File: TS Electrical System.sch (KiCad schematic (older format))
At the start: 29 parts

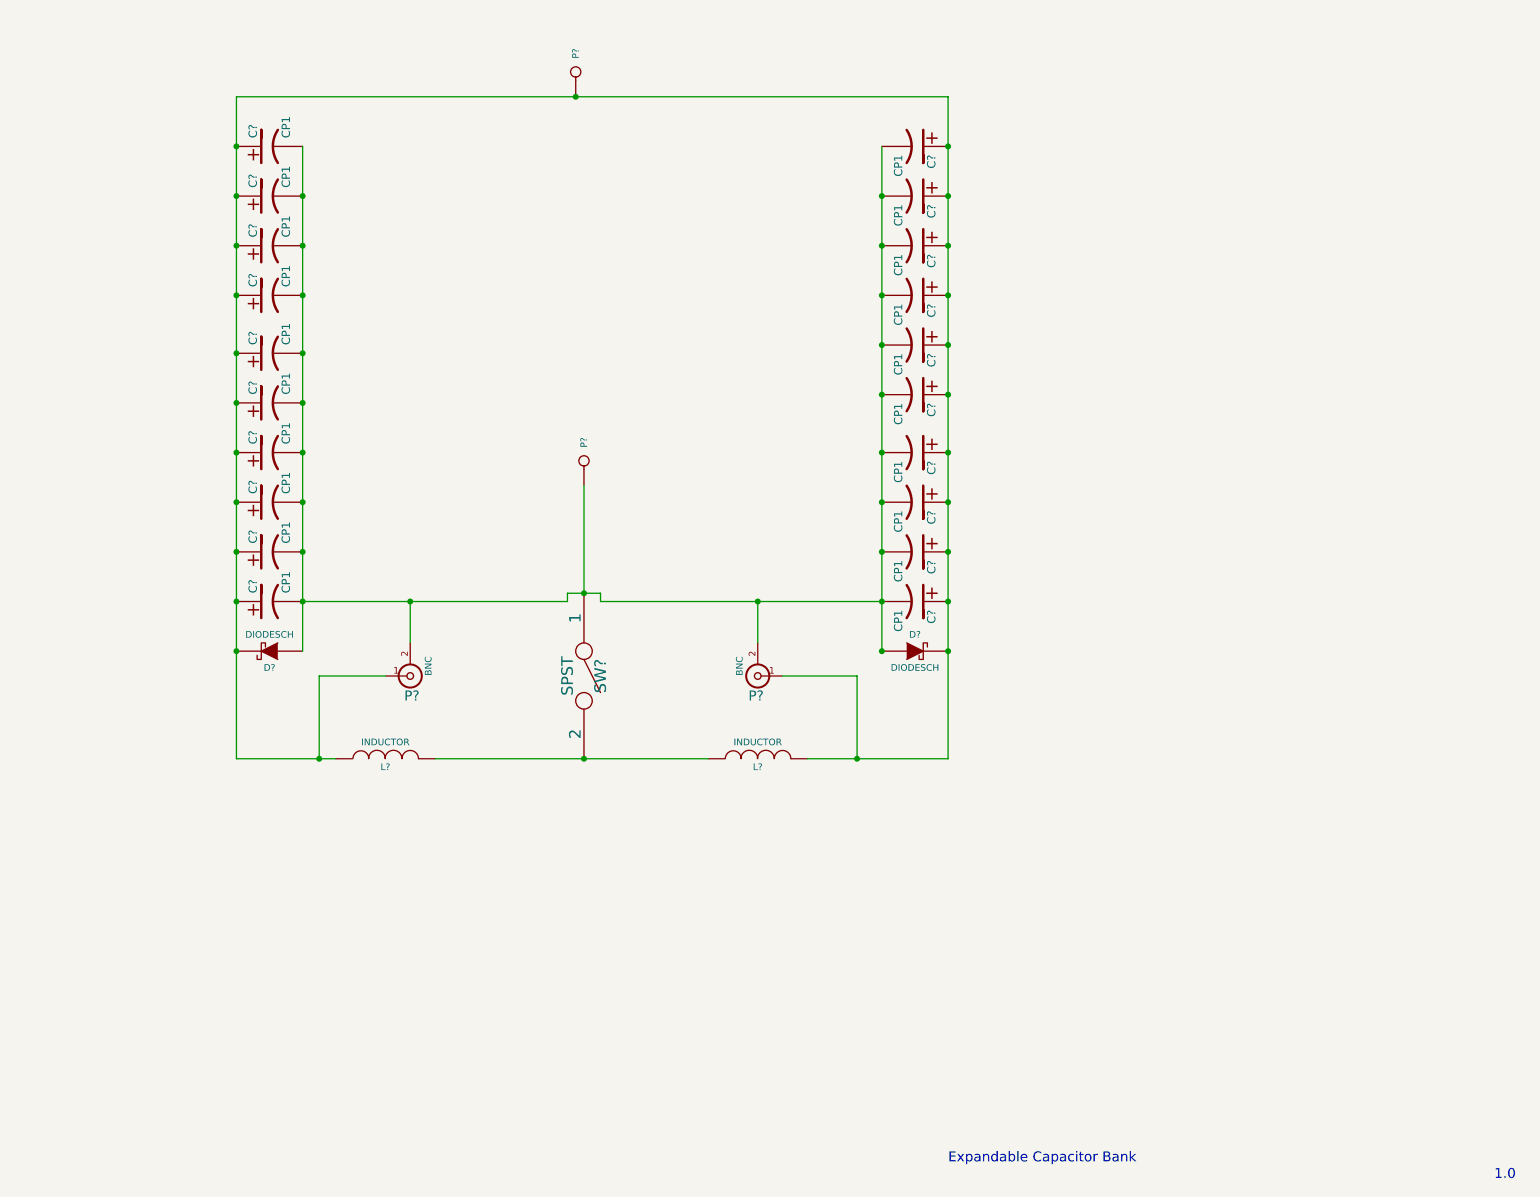
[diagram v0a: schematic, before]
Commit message: Associated Parts with Footprints, created footprints, and did part layout.
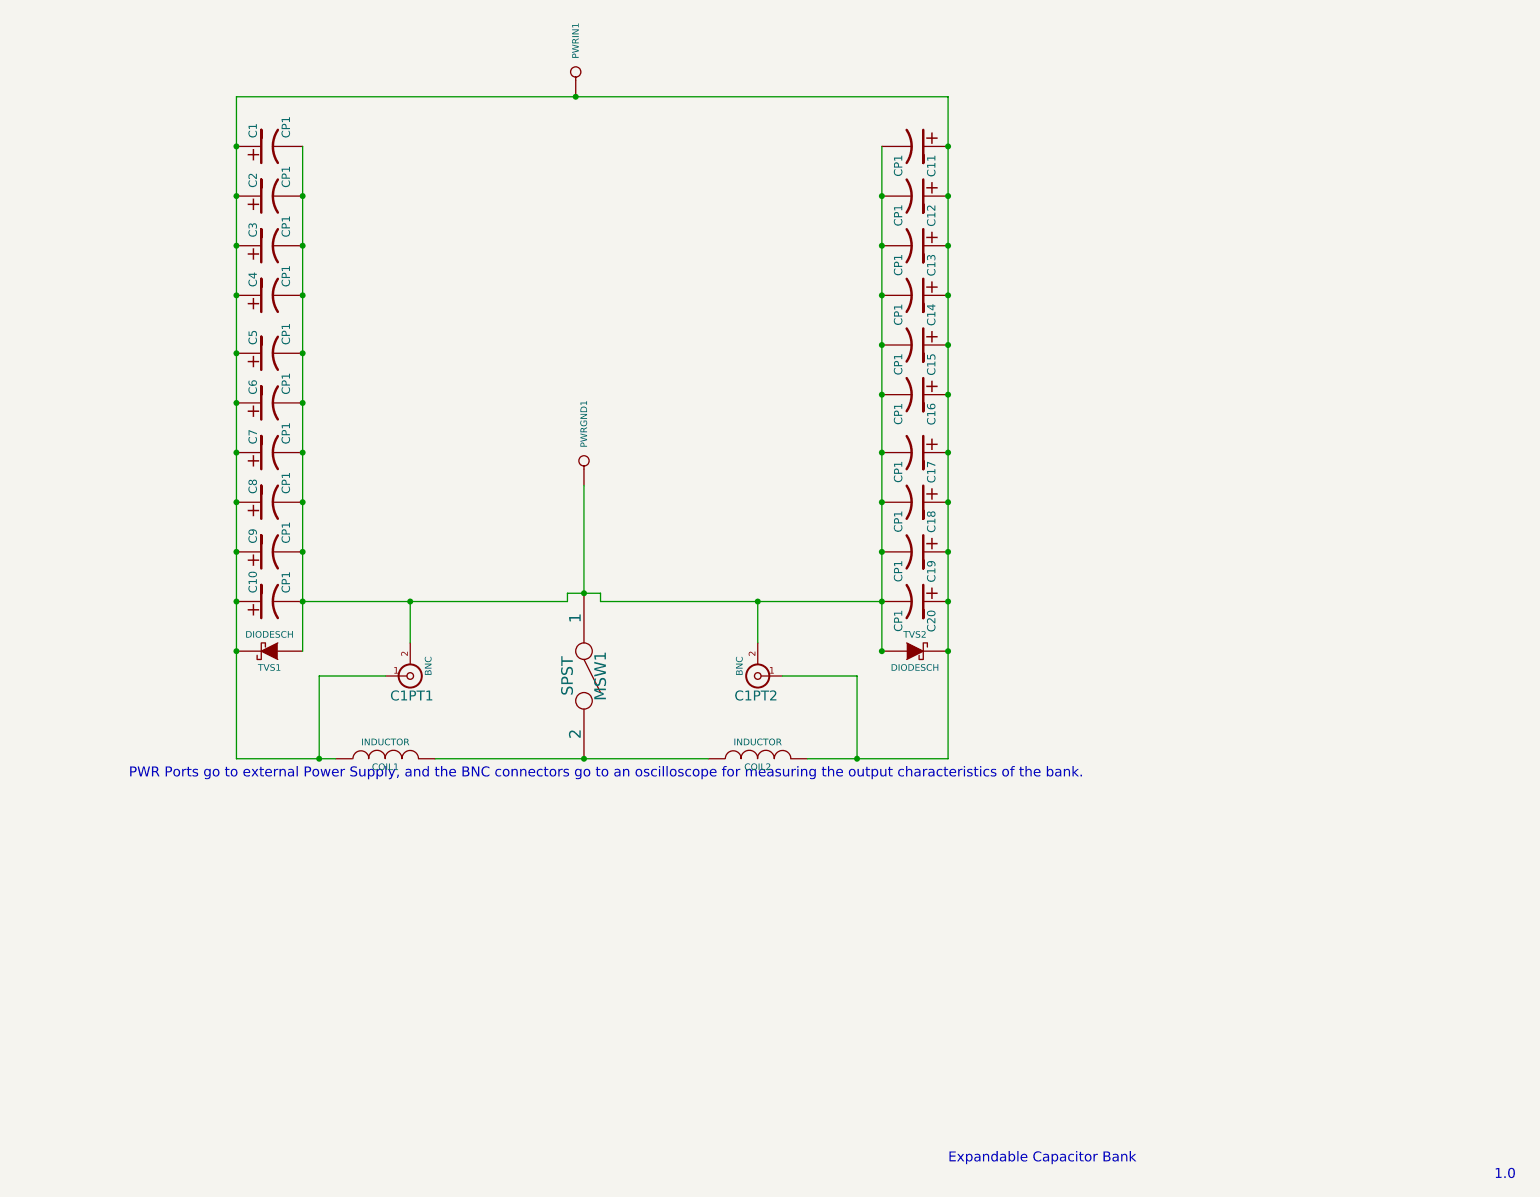
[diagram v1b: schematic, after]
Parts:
- gave numbers to parts that had none: 29
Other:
- note added: "PWR Ports go to external Power Supply, and the BNC connectors go to an oscilloscope for measuring the output characteristics of the bank.\n\n\n\n\n\n\n\n"
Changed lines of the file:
@@
-EESchema Schematic File Version 2  date Wed 30 Jul 2014 05:31:54 PM EDT
+EESchema Schematic File Version 2  date Wed 30 Jul 2014 05:36:56 PM EDT
 LIBS:power
 LIBS:device
@@
 Comment4 ""
 $EndDescr
+Text Notes 2400 5900 0    60   ~ 0
+PWR Ports go to external Power Supply, and the BNC connectors go to an oscilloscope for measuring the output characteristics of the bank.\n\n\n\n\n\n\n\n
 Connection ~ 5100 1100
 Connection ~ 3050 1400
@@
 	5150 3450 5150 4100
 $Comp
-L CONN_1 P?
+L CONN_1 PWRIN1
 U 1 1 53D96425
 P 5100 950
-F 0 "P?" H 5180 950 40  0000 L CNN
+F 0 "PWRIN1" H 5180 950 40  0000 L CNN
 F 1 "CONN_1" H 5100 1005 30  0001 C CNN
 	1    5100 950
@@
 $EndComp
 $Comp
-L CONN_1 P?
+L CONN_1 PWRGND1
 U 1 1 53D9641D
 P 5150 3300
-F 0 "P?" H 5230 3300 40  0000 L CNN
+F 0 "PWRGND1" H 5230 3300 40  0000 L CNN
 F 1 "CONN_1" H 5150 3355 30  0001 C CNN
 	1    5150 3300
@@
 1.0
 $Comp
-L BNC P?
+L BNC C1PT1
 U 1 1 53D9628A
 P 4100 4600
-F 0 "P?" H 4110 4720 60  0000 C CNN
+F 0 "C1PT1" H 4110 4720 60  0000 C CNN
 F 1 "BNC" V 4210 4540 40  0000 C CNN
 	1    4100 4600
@@
 $EndComp
 $Comp
-L BNC P?
+L BNC C1PT2
 U 1 1 53D9627A
 P 6200 4600
-F 0 "P?" H 6210 4720 60  0000 C CNN
+F 0 "C1PT2" H 6210 4720 60  0000 C CNN
 F 1 "BNC" V 6310 4540 40  0000 C CNN
 	1    6200 4600
@@
 $EndComp
 $Comp
-L SPST SW?
+L SPST MSW1
 U 1 1 53D96065
 P 5150 4600
-F 0 "SW?" H 5150 4700 70  0000 C CNN
+F 0 "MSW1" H 5150 4700 70  0000 C CNN
 F 1 "SPST" H 5150 4500 70  0000 C CNN
 	1    5150 4600
@@
 $EndComp
 $Comp
-L INDUCTOR L?
+L INDUCTOR COIL1
 U 1 1 53D961F9
 P 3950 5100
-F 0 "L?" V 3900 5100 40  0000 C CNN
+F 0 "COIL1" V 3900 5100 40  0000 C CNN
 F 1 "INDUCTOR" V 4050 5100 40  0000 C CNN
 	1    3950 5100
@@
 $EndComp
 $Comp
-L INDUCTOR L?
+L INDUCTOR COIL2
 U 1 1 53D961EB
 P 6200 5100
-F 0 "L?" V 6150 5100 40  0000 C CNN
+F 0 "COIL2" V 6150 5100 40  0000 C CNN
 F 1 "INDUCTOR" V 6300 5100 40  0000 C CNN
 	1    6200 5100
@@
 $EndComp
 $Comp
-L DIODESCH D?
+L DIODESCH TVS2
 U 1 1 53D96017
 P 7150 4450
-F 0 "D?" H 7150 4550 40  0000 C CNN
+F 0 "TVS2" H 7150 4550 40  0000 C CNN
 F 1 "DIODESCH" H 7150 4350 40  0000 C CNN
 	1    7150 4450
@@
 $EndComp
 $Comp
-L DIODESCH D?
+L DIODESCH TVS1
 U 1 1 53D9600F
 P 3250 4450
-F 0 "D?" H 3250 4550 40  0000 C CNN
+F 0 "TVS1" H 3250 4550 40  0000 C CNN
 F 1 "DIODESCH" H 3250 4350 40  0000 C CNN
 	1    3250 4450
@@
 $EndComp
 $Comp
-L CP1 C?
+L CP1 C20
 U 1 1 53D95FE6
 P 7150 4150
-F 0 "C?" H 7200 4250 50  0000 L CNN
+F 0 "C20" H 7200 4250 50  0000 L CNN
 F 1 "CP1" H 7200 4050 50  0000 L CNN
 	1    7150 4150
@@
 $EndComp
 $Comp
-L CP1 C?
+L CP1 C19
 U 1 1 53D95FE5
 P 7150 3850
-F 0 "C?" H 7200 3950 50  0000 L CNN
+F 0 "C19" H 7200 3950 50  0000 L CNN
 F 1 "CP1" H 7200 3750 50  0000 L CNN
 	1    7150 3850
@@
 $EndComp
 $Comp
-L CP1 C?
+L CP1 C17
 U 1 1 53D95FE4
 P 7150 3250
-F 0 "C?" H 7200 3350 50  0000 L CNN
+F 0 "C17" H 7200 3350 50  0000 L CNN
 F 1 "CP1" H 7200 3150 50  0000 L CNN
 	1    7150 3250
@@
 $EndComp
 $Comp
-L CP1 C?
+L CP1 C18
 U 1 1 53D95FE3
 P 7150 3550
-F 0 "C?" H 7200 3650 50  0000 L CNN
+F 0 "C18" H 7200 3650 50  0000 L CNN
 F 1 "CP1" H 7200 3450 50  0000 L CNN
 	1    7150 3550
@@
 $EndComp
 $Comp
-L CP1 C?
+L CP1 C14
 U 1 1 53D95FE2
 P 7150 2300
-F 0 "C?" H 7200 2400 50  0000 L CNN
+F 0 "C14" H 7200 2400 50  0000 L CNN
 F 1 "CP1" H 7200 2200 50  0000 L CNN
 	1    7150 2300
@@
 $EndComp
 $Comp
-L CP1 C?
+L CP1 C13
 U 1 1 53D95FE1
 P 7150 2000
-F 0 "C?" H 7200 2100 50  0000 L CNN
+F 0 "C13" H 7200 2100 50  0000 L CNN
 F 1 "CP1" H 7200 1900 50  0000 L CNN
 	1    7150 2000
@@
 $EndComp
 $Comp
-L CP1 C?
+L CP1 C15
 U 1 1 53D95FE0
 P 7150 2600
-F 0 "C?" H 7200 2700 50  0000 L CNN
+F 0 "C15" H 7200 2700 50  0000 L CNN
 F 1 "CP1" H 7200 2500 50  0000 L CNN
 	1    7150 2600
@@
 $EndComp
 $Comp
-L CP1 C?
+L CP1 C16
 U 1 1 53D95FDF
 P 7150 2900
-F 0 "C?" H 7200 3000 50  0000 L CNN
+F 0 "C16" H 7200 3000 50  0000 L CNN
 F 1 "CP1" H 7200 2800 50  0000 L CNN
 	1    7150 2900
@@
 $EndComp
 $Comp
-L CP1 C?
+L CP1 C11
 U 1 1 53D95FDE
 P 7150 1400
-F 0 "C?" H 7200 1500 50  0000 L CNN
+F 0 "C11" H 7200 1500 50  0000 L CNN
 F 1 "CP1" H 7200 1300 50  0000 L CNN
 	1    7150 1400
@@
 $EndComp
 $Comp
-L CP1 C?
+L CP1 C12
 U 1 1 53D95FDD
 P 7150 1700
-F 0 "C?" H 7200 1800 50  0000 L CNN
+F 0 "C12" H 7200 1800 50  0000 L CNN
 F 1 "CP1" H 7200 1600 50  0000 L CNN
 	1    7150 1700
@@
 $EndComp
 $Comp
-L CP1 C?
+L CP1 C9
 U 1 1 53D95FC9
 P 3250 3850
-F 0 "C?" H 3300 3950 50  0000 L CNN
+F 0 "C9" H 3300 3950 50  0000 L CNN
 F 1 "CP1" H 3300 3750 50  0000 L CNN
 	1    3250 3850
@@
 $EndComp
 $Comp
-L CP1 C?
+L CP1 C10
 U 1 1 53D95FC8
 P 3250 4150
-F 0 "C?" H 3300 4250 50  0000 L CNN
+F 0 "C10" H 3300 4250 50  0000 L CNN
 F 1 "CP1" H 3300 4050 50  0000 L CNN
 	1    3250 4150
@@
 $EndComp
 $Comp
-L CP1 C?
+L CP1 C5
 U 1 1 53D95FC1
 P 3250 2650
-F 0 "C?" H 3300 2750 50  0000 L CNN
+F 0 "C5" H 3300 2750 50  0000 L CNN
 F 1 "CP1" H 3300 2550 50  0000 L CNN
 	1    3250 2650
@@
 $EndComp
 $Comp
-L CP1 C?
+L CP1 C6
 U 1 1 53D95FC0
 P 3250 2950
-F 0 "C?" H 3300 3050 50  0000 L CNN
+F 0 "C6" H 3300 3050 50  0000 L CNN
 F 1 "CP1" H 3300 2850 50  0000 L CNN
 	1    3250 2950
@@
 $EndComp
 $Comp
-L CP1 C?
+L CP1 C8
 U 1 1 53D95FBF
 P 3250 3550
-F 0 "C?" H 3300 3650 50  0000 L CNN
+F 0 "C8" H 3300 3650 50  0000 L CNN
 F 1 "CP1" H 3300 3450 50  0000 L CNN
 	1    3250 3550
@@
 $EndComp
 $Comp
-L CP1 C?
+L CP1 C7
 U 1 1 53D95FBE
 P 3250 3250
-F 0 "C?" H 3300 3350 50  0000 L CNN
+F 0 "C7" H 3300 3350 50  0000 L CNN
 F 1 "CP1" H 3300 3150 50  0000 L CNN
 	1    3250 3250
@@
 $EndComp
 $Comp
-L CP1 C?
+L CP1 C3
 U 1 1 53D95FB5
 P 3250 2000
-F 0 "C?" H 3300 2100 50  0000 L CNN
+F 0 "C3" H 3300 2100 50  0000 L CNN
 F 1 "CP1" H 3300 1900 50  0000 L CNN
 	1    3250 2000
@@
 $EndComp
 $Comp
-L CP1 C?
+L CP1 C4
 U 1 1 53D95FB4
 P 3250 2300
-F 0 "C?" H 3300 2400 50  0000 L CNN
+F 0 "C4" H 3300 2400 50  0000 L CNN
 F 1 "CP1" H 3300 2200 50  0000 L CNN
 	1    3250 2300
@@
 $EndComp
 $Comp
-L CP1 C?
+L CP1 C2
 U 1 1 53D95FAB
 P 3250 1700
-F 0 "C?" H 3300 1800 50  0000 L CNN
+F 0 "C2" H 3300 1800 50  0000 L CNN
 F 1 "CP1" H 3300 1600 50  0000 L CNN
 	1    3250 1700
@@
 $EndComp
 $Comp
-L CP1 C?
+L CP1 C1
 U 1 1 53D95FA0
 P 3250 1400
-F 0 "C?" H 3300 1500 50  0000 L CNN
+F 0 "C1" H 3300 1500 50  0000 L CNN
 F 1 "CP1" H 3300 1300 50  0000 L CNN
 	1    3250 1400

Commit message: Version 2.0 of the board using the terminal blocks that Steve gave me. It is a single sided board since the terminal connectors are only able to connect on one side of the board. Had to revise the schematic slightly to account for the flyback diode net.
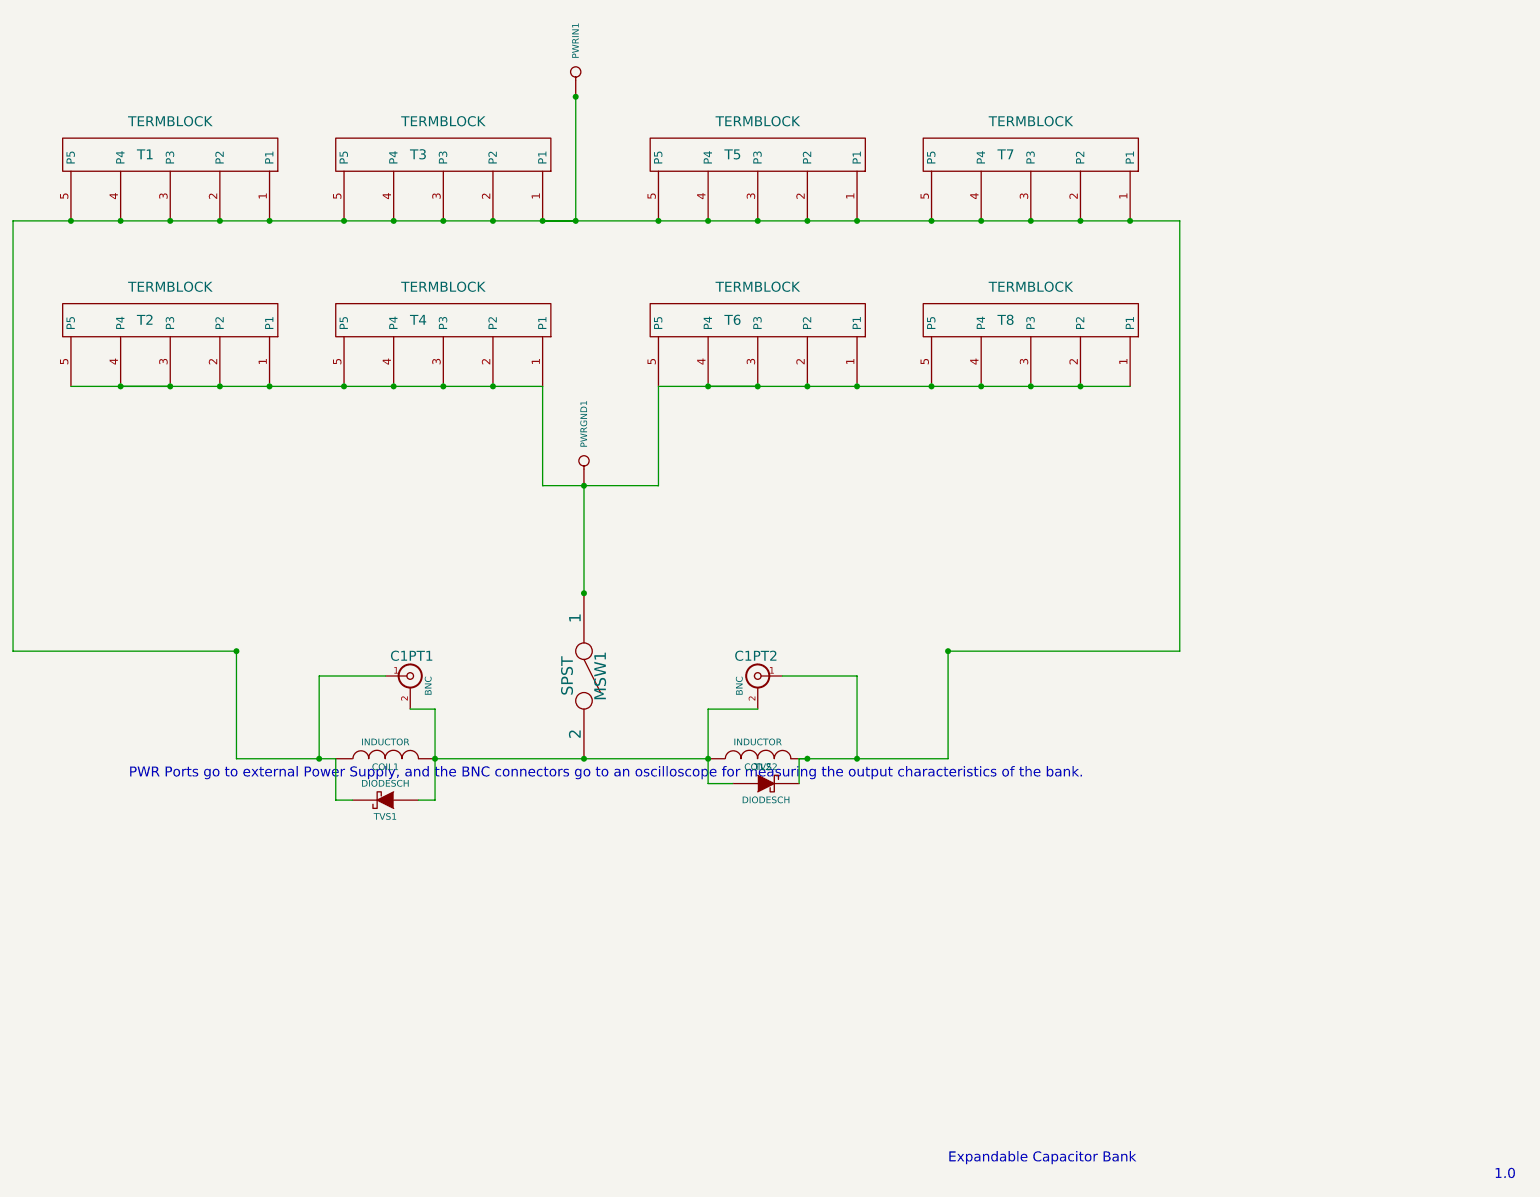
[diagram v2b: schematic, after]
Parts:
- removed C1, C10, C11, C12, C13, C14, C15, C16, C17, C18, C19, C2, C20, C3, C4, C5, C6, C7, C8, C9: CP1, symbol CP1
- added T1, T2, T3, T4, T5, T6, T7, T8: TERMBLOCK, symbol TERMBLOCK
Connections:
- net at C1PT1.1 (In), C1PT2.1 (In), COIL1.1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: now also T1.1 (P1), T1.2 (P2), T1.3 (P3), T1.4 (P4), T1.5 (P5), T1.~, T3.1 (P1), T3.2 (P2), T3.3 (P3), T3.4 (P4), T3.5 (P5), T3.~, T5.1 (P1), T5.2 (P2), T5.3 (P3), T5.4 (P4), T5.5 (P5), T5.~, T7.1 (P1), T7.2 (P2), T7.3 (P3), T7.4 (P4), T7.5 (P5), T7.~
- net at C1PT1.2 (Ext), C1PT2.2 (Ext), TVS1.1 (A)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: now also COIL1.2, COIL2.1, MSW1.2; no longer MSW1.1, PWRGND1.1
- new net: MSW1.1, PWRGND1.1, T2.1 (P1), T2.2 (P2), T2.3 (P3), T2.4 (P4), T2.5 (P5), T2.~, T4.1 (P1), T4.2 (P2), T4.3 (P3), T4.4 (P4), T4.5 (P5), T4.~, T6.1 (P1), T6.2 (P2), T6.3 (P3), T6.4 (P4), T6.5 (P5), T6.~, T8.1 (P1), T8.2 (P2), T8.3 (P3), T8.4 (P4), T8.5 (P5), T8.~
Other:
- moved on the sheet: C1PT1, C1PT2, TVS1, TVS2
